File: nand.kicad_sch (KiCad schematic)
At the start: 0 parts

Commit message: Added Power Nand USB
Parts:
- added C50: 100n, symbol SparkFun-Capacitor:C
- added R17, R18, R19: 10k, symbol SparkFun-Resistor:R
- added U4: IS21ES08GA-JQLI-TR, FBGA100_ISI, symbol IS21ES08GA_JQLI_TR:IS21ES08GA-JQLI-TR
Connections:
- new net CLK: R18.2, U4.P6 (CLK)
- new net CMD: R17.2, U4.P5 (CMD)
- new net GND: U4.G2 (VSS), U4.G3 (VSS), U4.G4 (VSS), U4.G5 (VSS), U4.G6 (VSS), U4.G7 (VSS), U4.G8 (VSS), U4.G9 (VSS), U4.H2 (VSSQ), U4.H9 (VSSQ), U4.J5 (VSSQ), U4.L3 (VSSQ), U4.L8 (VSSQ), U4.M4 (VSSQ), U4.M7 (VSSQ), U4.P2 (VSSQ), U4.P9 (VSSQ)
- new net NAND0: R19.2, U4.K2 (DAT_0)
- new net NAND1: U4.N2 (DAT_1)
- new net NAND2: U4.K3 (DAT_2)
- new net NAND3: U4.N3 (DAT_3)
- new net NAND4: U4.N8 (DAT_4)
- new net NAND5: U4.K8 (DAT_5)
- new net NAND6: U4.N9 (DAT_6)
- new net NAND7: U4.K9 (DAT_7)
- new net RESET: U4.M5 (RST__N)
- new net VDD: R17.1, R18.1, R19.1, U4.F2 (VCC), U4.F3 (VCC), U4.F4 (VCC), U4.F5 (VCC), U4.F6 (VCC), U4.F7 (VCC), U4.F8 (VCC), U4.F9 (VCC), U4.H3 (VCCQ), U4.H8 (VCCQ), U4.L2 (VCCQ), U4.L4 (VCCQ), U4.L7 (VCCQ), U4.L9 (VCCQ), U4.P3 (VCCQ), U4.P8 (VCCQ)
- new net VDDI: U4.E4 (VDDI)
- no-connect marks 0 -> 1

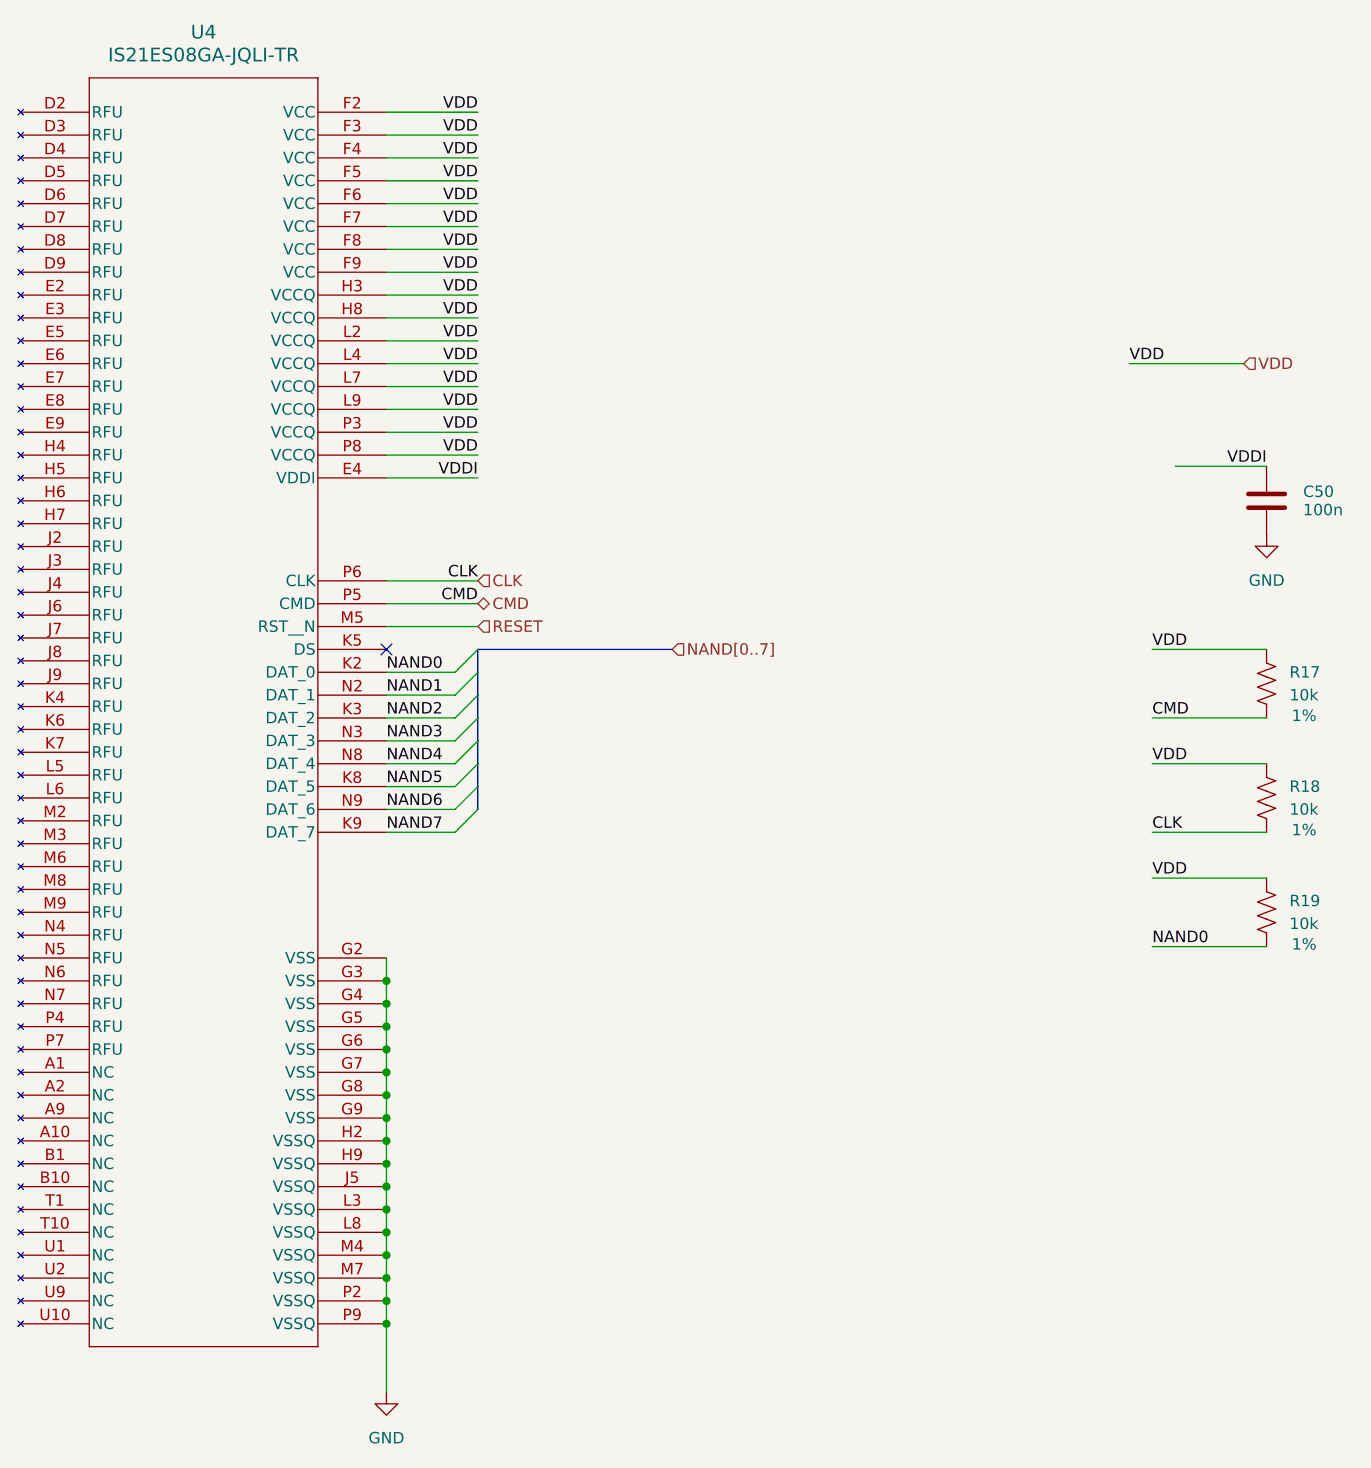
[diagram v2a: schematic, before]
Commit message: Adding more decoupling and started on DSI connector
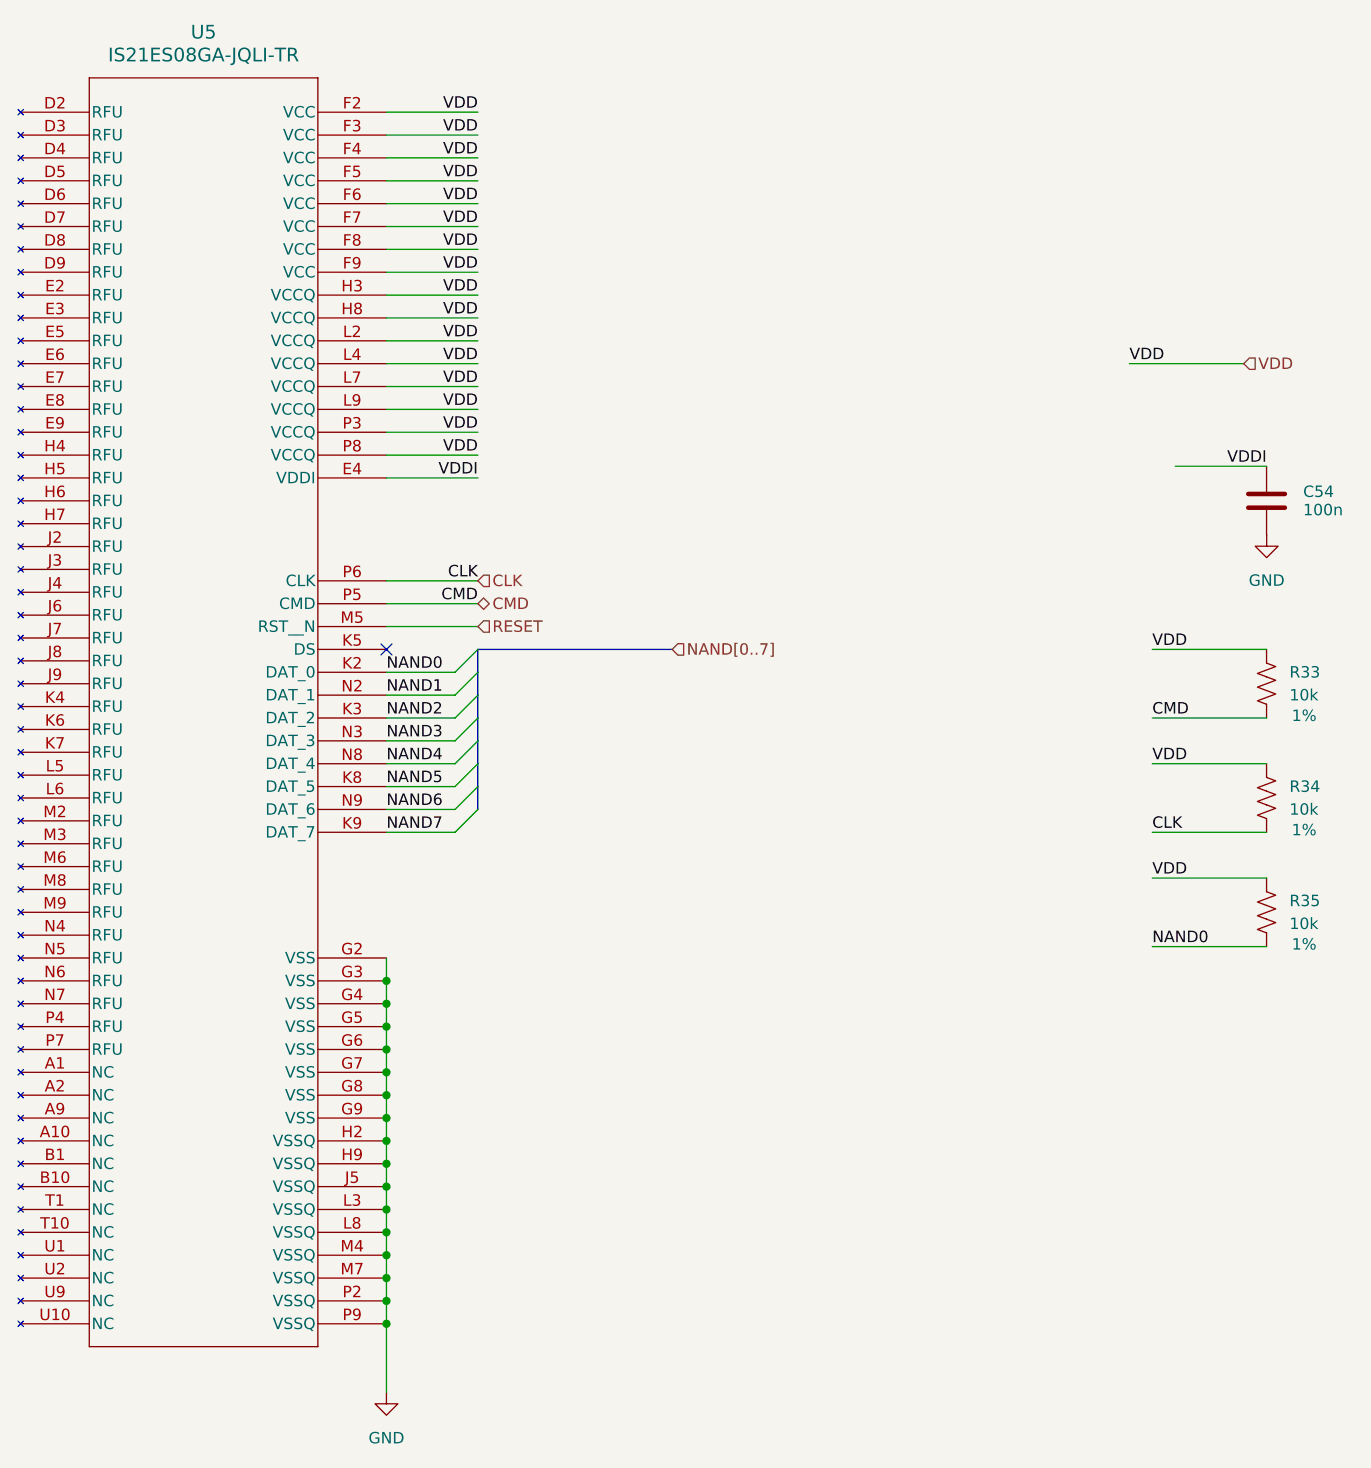
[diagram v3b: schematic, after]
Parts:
- U5: renamed from U4; footprint FBGA100_ISI -> (none)
- renumbered C50 to C54, R17 to R33, R18 to R34, R19 to R35
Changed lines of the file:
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@@
 		(on_board yes)
 		(dnp no)
-		(property "Reference" "R18"
+		(property "Reference" "R34"
 			(at 259.08 106.6799 90)
 			(effects
@@
 			(project "SBC"
 				(path "/21bb932a-ec67-4661-9215-0551f718d1c0/dbc4538f-6782-4334-8773-c54462e4bd8b"
-					(reference "R18")
+					(reference "R34")
 					(unit 1)
 				)
@@
 		(on_board yes)
 		(dnp no)
-		(property "Reference" "R19"
+		(property "Reference" "R35"
 			(at 259.08 119.3799 90)
 			(effects
@@
 			(project "SBC"
 				(path "/21bb932a-ec67-4661-9215-0551f718d1c0/dbc4538f-6782-4334-8773-c54462e4bd8b"
-					(reference "R19")
+					(reference "R35")
 					(unit 1)
 				)
@@
 		(on_board yes)
 		(dnp no)
-		(property "Reference" "C50"
+		(property "Reference" "C54"
 			(at 260.604 73.914 0)
 			(effects
@@
 			(project "SBC"
 				(path "/21bb932a-ec67-4661-9215-0551f718d1c0/dbc4538f-6782-4334-8773-c54462e4bd8b"
-					(reference "C50")
+					(reference "C54")
 					(unit 1)
 				)
@@
 		(dnp no)
 		(fields_autoplaced yes)
-		(property "Reference" "#PWR098"
+		(property "Reference" "#PWR0116"
 			(at 256.5518 85.0547 0)
 			(effects
@@
 			(project "SBC"
 				(path "/21bb932a-ec67-4661-9215-0551f718d1c0/dbc4538f-6782-4334-8773-c54462e4bd8b"
-					(reference "#PWR098")
+					(reference "#PWR0116")
 					(unit 1)
 				)
@@
 		(on_board yes)
 		(dnp no)
-		(property "Reference" "R17"
+		(property "Reference" "R33"
 			(at 259.08 93.9799 90)
 			(effects
@@
 			(project "SBC"
 				(path "/21bb932a-ec67-4661-9215-0551f718d1c0/dbc4538f-6782-4334-8773-c54462e4bd8b"
-					(reference "R17")
+					(reference "R33")
 					(unit 1)
 				)
@@
 		(dnp no)
 		(fields_autoplaced yes)
-		(property "Reference" "U4"
+		(property "Reference" "U5"
 			(at 138.43 22.86 0)
 			(effects
@@
 			)
 		)
-		(property "Footprint" "FBGA100_ISI"
+		(property "Footprint" ""
 			(at 138.43 170.434 0)
 			(effects
@@
 			(project ""
 				(path "/21bb932a-ec67-4661-9215-0551f718d1c0/dbc4538f-6782-4334-8773-c54462e4bd8b"
-					(reference "U4")
+					(reference "U5")
 					(unit 1)
 				)
@@
 		(dnp no)
 		(fields_autoplaced yes)
-		(property "Reference" "#PWR097"
+		(property "Reference" "#PWR0117"
 			(at 158.75 180.34 0)
 			(effects
@@
 			(project ""
 				(path "/21bb932a-ec67-4661-9215-0551f718d1c0/dbc4538f-6782-4334-8773-c54462e4bd8b"
-					(reference "#PWR097")
+					(reference "#PWR0117")
 					(unit 1)
 				)

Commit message: Adding another usb and cleanup
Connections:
- net VDD: now also U5.E4 (VDDI)
- net VDDI: no longer U5.E4 (VDDI)
